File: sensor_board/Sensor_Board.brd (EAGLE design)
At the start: 73.6 x 26.3 mm, 9 parts, among them J1 SL04, J2 SL03THROUGH_HOLE, J3 SL04, J4 SL03THROUGH_HOLE, J5 SL03THROUGH_HOLE

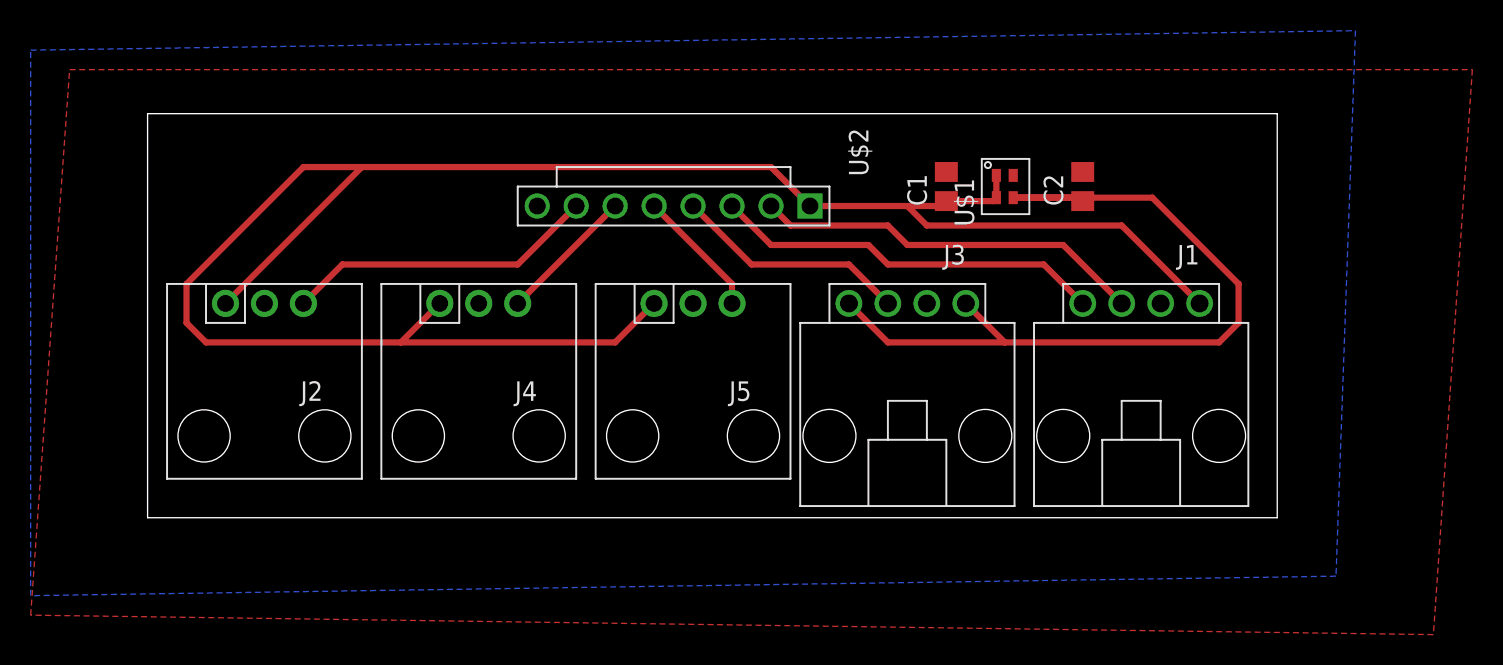
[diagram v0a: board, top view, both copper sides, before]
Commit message: Weather and Soil Sensor boards
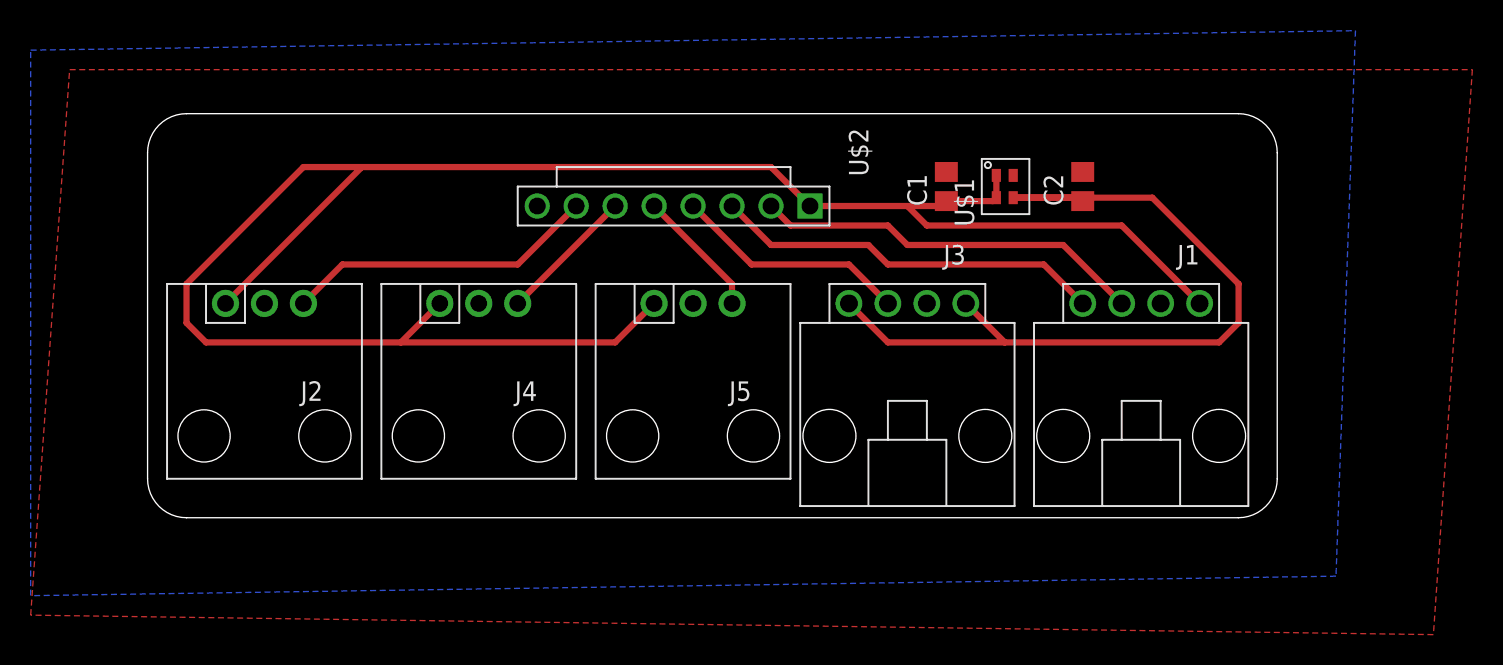
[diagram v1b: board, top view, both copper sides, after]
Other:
- outline, holes or cut-outs redrawn
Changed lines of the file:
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@@
 <layer number="25" name="tNames" color="7" fill="1" visible="yes" active="yes"/>
 <layer number="26" name="bNames" color="7" fill="1" visible="yes" active="yes"/>
-<layer number="27" name="tValues" color="7" fill="1" visible="yes" active="yes"/>
-<layer number="28" name="bValues" color="7" fill="1" visible="yes" active="yes"/>
+<layer number="27" name="tValues" color="7" fill="1" visible="no" active="yes"/>
+<layer number="28" name="bValues" color="7" fill="1" visible="no" active="yes"/>
 <layer number="29" name="tStop" color="7" fill="3" visible="no" active="yes"/>
 <layer number="30" name="bStop" color="7" fill="6" visible="no" active="yes"/>
@@
 <board>
 <plain>
-<wire x1="0" y1="0" x2="73.64" y2="0" width="0" layer="20"/>
-<wire x1="73.64" y1="0" x2="73.64" y2="26.34" width="0" layer="20"/>
-<wire x1="73.64" y1="26.34" x2="0" y2="26.34" width="0" layer="20"/>
-<wire x1="0" y1="26.34" x2="0" y2="0" width="0" layer="20"/>
+<wire x1="0" y1="23.8" x2="0" y2="2.54" width="0" layer="20"/>
+<wire x1="0" y1="2.54" x2="2.54" y2="0" width="0" layer="20" curve="90"/>
+<wire x1="2.54" y1="0" x2="71.1" y2="0" width="0" layer="20"/>
+<wire x1="71.1" y1="0" x2="73.64" y2="2.54" width="0" layer="20" curve="90"/>
+<wire x1="73.64" y1="2.54" x2="73.64" y2="23.8" width="0" layer="20"/>
+<wire x1="73.64" y1="23.8" x2="71.1" y2="26.34" width="0" layer="20" curve="90"/>
+<wire x1="71.1" y1="26.34" x2="2.54" y2="26.34" width="0" layer="20"/>
+<wire x1="2.54" y1="26.34" x2="0" y2="23.8" width="0" layer="20" curve="90"/>
 </plain>
 <attributes>
